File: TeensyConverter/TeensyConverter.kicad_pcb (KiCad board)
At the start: 2 copper layers, 5 parts, among them P1 CONN_01X03, U1 Teensy-3.2, U2 CE_HEADER

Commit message: 1st pass at layout
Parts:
- U1: moved to B.Cu
- moved R1 39.4 mm to (144.9, 106.0), turned to 90 degrees
- moved R2 31.4 mm to (146.3, 111.9), turned to 270 degrees
- moved U2 28.4 mm to (151.5, 122.4), turned to 180 degrees
- moved P1 16.8 mm to (148.1, 94.1), turned to 90 degrees
- moved U1 3.70 mm to (150.1, 108.3), turned to 180 degrees
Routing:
- net /AIO1: track 0.00 -> 24.9 mm
- net /AIO0: track 0.00 -> 22.0 mm
- net /AIO3: track 0.00 -> 21.8 mm
- net /AIO2: track 0.00 -> 20.4 mm
- net /TEENSY_RX: track 0.00 -> 17.5 mm
- net /DEVICE_RX: track 0.00 -> 15.1 mm
- net /I2C_SDAT: track 0.00 -> 12.7 mm
- net /3.3V: track 0.00 -> 12.2 mm
- net /SPI_CLK: track 0.00 -> 11.6 mm
- net /SPI_MOSI: track 0.00 -> 10.5 mm
- net /I2C_SCLK: track 0.00 -> 9.01 mm
- net /TEENSY_TX: track 0.00 -> 8.34 mm
- net /5V: track 0.00 -> 4.99 mm
- net /DEVICE_TX: track 0.00 -> 3.79 mm
- net /SPI_CS: track 0.00 -> 0.63 mm
- added copper zone on B.Cu, net /GND
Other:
- net class Default: clearance 0.2 -> 0.1524; trace_width 0.25 -> 0.254; via_dia 0.6 -> 0.6858; via_drill 0.4 -> 0.3302
- rule trace_clearance: 0.2 -> 0.1524
- rule trace_min: 0.2 -> 0.1524
- rule via_min_drill: 0.3 -> 0.3302
- rule via_min_size: 0.4 -> 0.6858

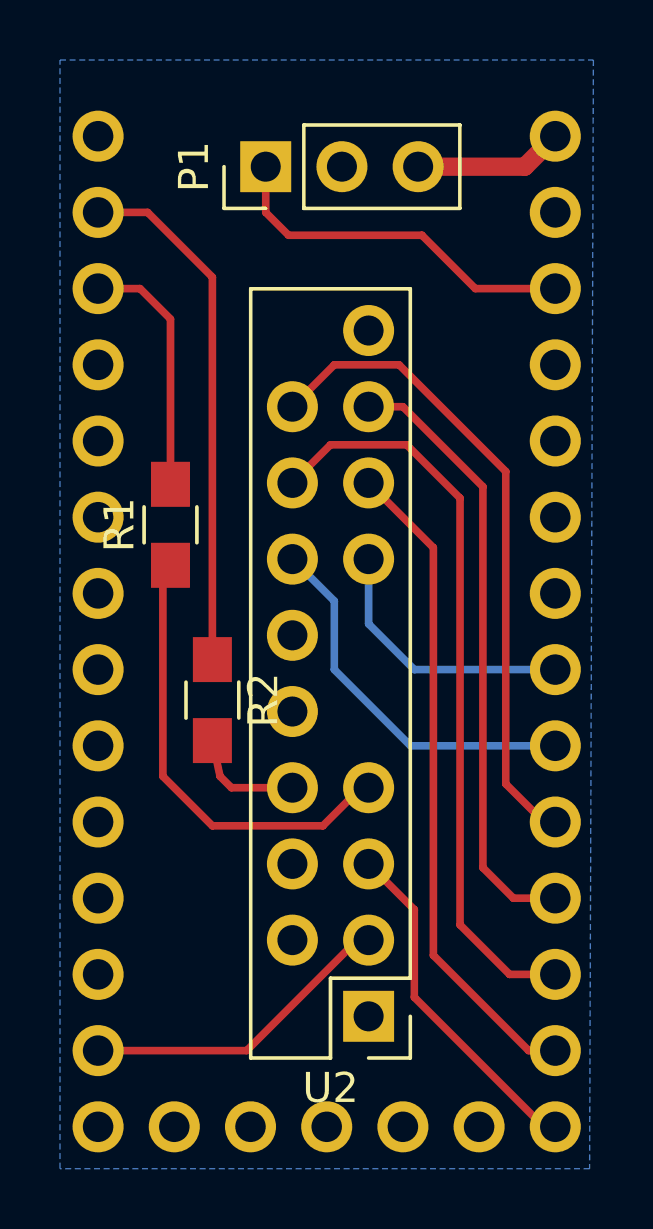
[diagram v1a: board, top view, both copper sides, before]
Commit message: Swapped CE header 180 degrees
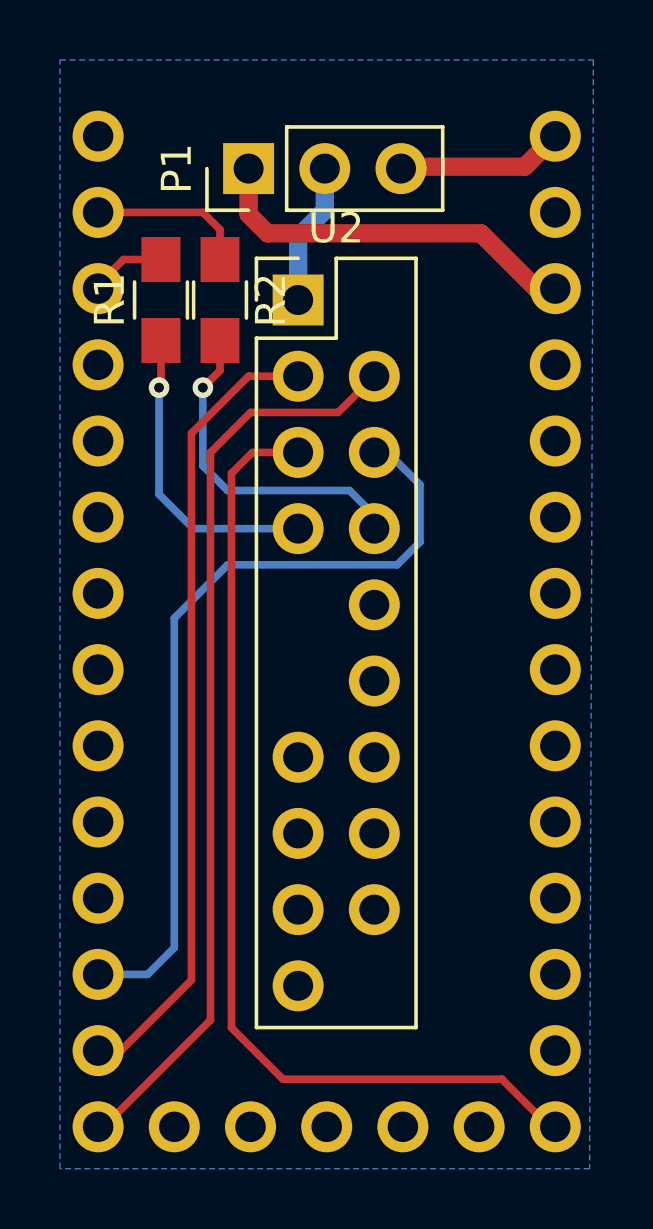
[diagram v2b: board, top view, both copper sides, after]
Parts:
- moved U2 24.0 mm to (149.2, 98.6), turned to 0 degrees
- moved R2 13.3 mm to (146.6, 98.6)
- moved R1 7.50 mm to (144.6, 98.6)
- moved P1 0.58 mm to (147.5, 94.2)
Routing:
- net /SPI_MISO: track 0.25 -> 30.7 mm
- net /SPI_CS: track 0.63 -> 27.0 mm
- net /AIO1: track 24.9 -> 0.00 mm
- net /AIO0: track 22.0 -> 0.00 mm
- net /AIO3: track 21.8 -> 0.00 mm
- net /SPI_CLK: track 11.6 -> 33.2 mm
- net /AIO2: track 20.4 -> 0.00 mm
- net /SPI_MOSI: track 10.5 -> 26.7 mm
- net /I2C_SDAT: track 12.7 -> 0.00 mm
- net /TEENSY_RX: track 17.5 -> 5.30 mm
- net /I2C_SCLK: track 9.01 -> 0.00 mm
- net /DEVICE_TX: track 3.79 -> 11.3 mm, vias 0 -> 1
- net /TEENSY_TX: track 8.34 -> 2.57 mm
- net /DEVICE_RX: track 15.1 -> 10.3 mm, vias 0 -> 1
- net Net-(P1-Pad2): track 0.00 -> 4.75 mm
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
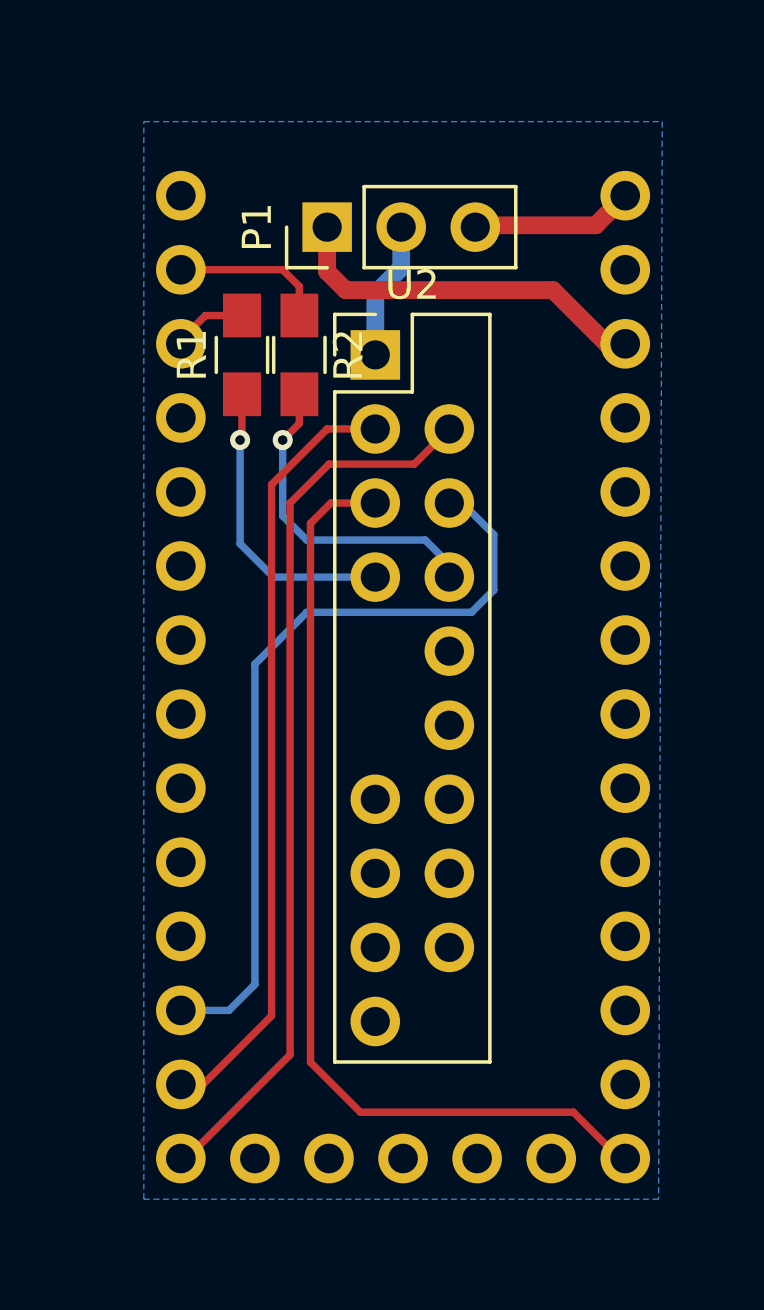
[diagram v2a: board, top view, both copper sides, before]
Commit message: Finished layout of CE header converter for Teensy with flipped footprints
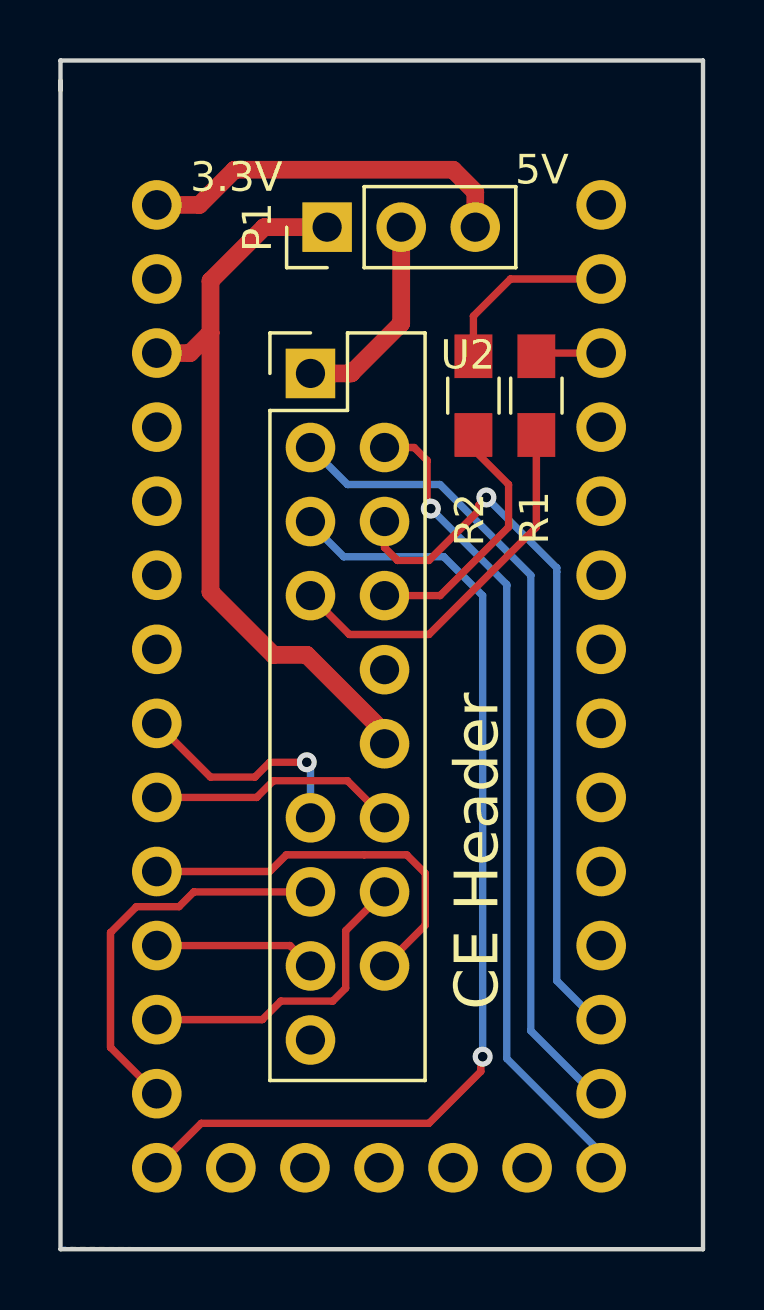
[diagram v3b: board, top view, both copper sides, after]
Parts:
- moved R1 10.2 mm to (154.7, 99.9)
- moved R2 6.13 mm to (152.5, 99.9)
- moved U2 2.31 mm to (146.9, 99.2)
- moved U1 0.88 mm to (149.3, 108.6)
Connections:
- U1 pad 30: Net-(U1-Pad30) -> /GND
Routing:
- net /AIO0: track 0.00 -> 13.6 mm
- net /AIO3: track 0.00 -> 13.5 mm
- net /3.3V: track 12.8 -> 25.9 mm
- net /AIO1: track 0.00 -> 10.8 mm
- net /I2C_SDAT: track 0.00 -> 8.57 mm
- net /I2C_SCLK: track 0.00 -> 8.07 mm, vias 0 -> 1
- net /5V: track 4.99 -> 12.9 mm
- net /AIO2: track 0.00 -> 5.56 mm
- net /DEVICE_RX: track 10.3 -> 13.0 mm, vias 1 -> 0
- net /SPI_CLK: track 33.2 -> 35.8 mm, vias 0 -> 1
- net Net-(P1-Pad2): track 4.75 -> 7.12 mm
- net /SPI_MISO: track 30.7 -> 28.4 mm, vias 0 -> 1
- net /SPI_MOSI: track 26.7 -> 28.4 mm
- net /DEVICE_TX: track 11.3 -> 9.52 mm, vias 1 -> 0
- net /SPI_CS: track 27.0 -> 25.3 mm, vias 0 -> 1
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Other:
- board outline added: 22 x 40.8 mm
- board text added: "3.3V"
- board text added: "5V"
- board text added: "CE Header"
- board text added: "Teensy"
